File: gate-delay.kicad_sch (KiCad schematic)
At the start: 42 parts, among them J1 Conn_02x05_Odd_Even, J2 gate_in, J3 gate_out, J4 gate_out, Q1 BCM847, Q2 BSS84, Q3 MMBF170, U1 TL072

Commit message: fix: try to maintain gate duration
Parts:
- added R17, R19, R21, R22: 10K, symbol Device:R
- added R18: 68K, symbol Device:R
- added R20: 50K, symbol Device:R
- R10: value 24K -> 1K
- R11: value 47K -> 10K
- R13: value 1K -> 68K
- R14: value 10K -> 50K
- R8: value 10K -> 110K
- R9: value 10K -> 22K
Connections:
- net +12V': now also R18.1; no longer R8.1
- net -12V': now also C3.2, Q3.2 (S)
- net GND': now also R11.2, U1.2 (-), R20.2, R21.1; no longer C3.2, Q3.2 (S), R9.2
- net at D4.1 (K), Q1.5 (B2): now also R10.2; no longer R13.1
- net at D4.2 (A), U1.1: now also R9.1; no longer R11.1
- net at R13.2, R14.1: now also R17.1; no longer R16.2
- net at C3.1, RV1.2, RV1.3: now also R13.1, R8.2; no longer R10.1, U1.5 (+)
- net at R15.2, U1.7: now also R22.2; no longer U1.6 (-)
- new net: R10.1, R11.1, R16.2
- new net: R8.1, R9.2, U1.3 (+)
- new net: R21.2, R22.1, U1.6 (-)
- new net: R18.2, R19.1, R20.1
- new net: R17.2, R19.2, U1.5 (+)
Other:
- moved on the sheet: R10, R11, R13, R14, R15, R8, R9, U1B

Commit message: feat: v0 pcb layed out
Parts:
- removed R15, R16: 1K, symbol Device:R
- removed R17, R19, R21, R22: 10K, symbol Device:R
- removed R18: 68K, symbol Device:R
- removed R20: 50K, symbol Device:R
- added H9: led, Eurorack:Mech-LED-Hole-3mm-Bezel, symbol Eurorack:MountingHole_Pad_Output
- C3: footprint (none) -> Capacitor_THT:C_Rect_L7.2mm_W5.5mm_P5.00mm_FKS2_FKP2_MKS2_MKP2
- C4: footprint (none) -> Capacitor_SMD:C_0805_2012Metric
- D3, D4: footprint (none) -> Diode_SMD:D_SOD-323_HandSoldering
- D5: footprint (none) -> LED_THT:LED_D3.0mm
- H8: value slew -> delay
- J2, J3: footprint (none) -> Eurorack:AudioJack2_Tayda_A-2566
- J4: value gate_out -> slew_out; footprint (none) -> Eurorack:AudioJack2_Tayda_A-2566
- Q2: footprint Package_TO_SOT_THT:TO-92_Inline -> Package_TO_SOT_SMD:SOT-23
- R10, R11, R12, R3, R4, R5, R6, R7, R8, R9: footprint (none) -> Resistor_SMD:R_0805_2012Metric
- R13: value 68K -> 1K; footprint (none) -> Resistor_SMD:R_0805_2012Metric
- R14: value 50K -> 1K; footprint (none) -> Resistor_SMD:R_0805_2012Metric
- RV1: footprint (none) -> Eurorack:Potentiometer_RV16AF-41-15R1
- U1: footprint (none) -> Package_SO:SOIC-8_3.9x4.9mm_P1.27mm
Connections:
- net +12V' is gone; now on net +12V: C4.1, Q1.3 (C2), Q2.2 (S), R5.1, U1.8 (V+)
- net +12V: now also R8.2
- net -12V: now also C4.2, U1.4 (V-)
- net FACE: now also H9.1
- net GATE_OUT': now also R13.1
- net GND: now also C3.2, D3.2 (A), J2.S, J3.S, J4.S, Q1.1 (E1), Q3.2 (S), R11.2, R12.2, R4.2, R9.1
- net SLEW_OUT': now also R14.1
- net at D4.2 (A), U1.1: no longer R9.1
- net at R10.1, R11.1: now also R13.2
- net at C3.1, RV1.2, RV1.3: now also U1.3 (+), U1.5 (+); no longer R13.1, R8.2
- net at R8.1, R9.2: now also U1.2 (-); no longer U1.3 (+)
- net at U1.6 (-): now also R14.2, U1.7
- removed net -12V': C3.2, C4.2, Q3.2 (S), U1.4 (V-)
- removed net GND': D3.2 (A), J2.S, J3.S, J4.S, Q1.1 (E1), R11.2, R12.2, R14.2, R4.2, U1.2 (-)
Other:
- moved on the sheet: R13, R14, R8, R9, U1B

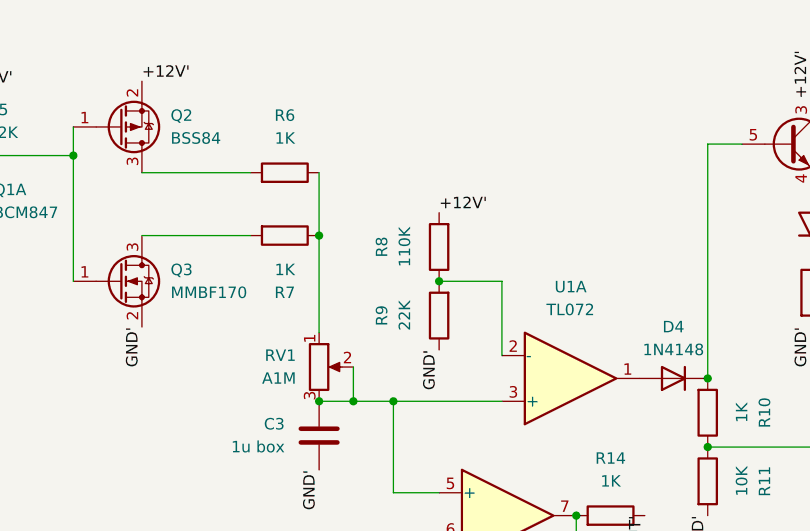
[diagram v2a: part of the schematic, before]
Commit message: v1 ready (uses the v0 board)
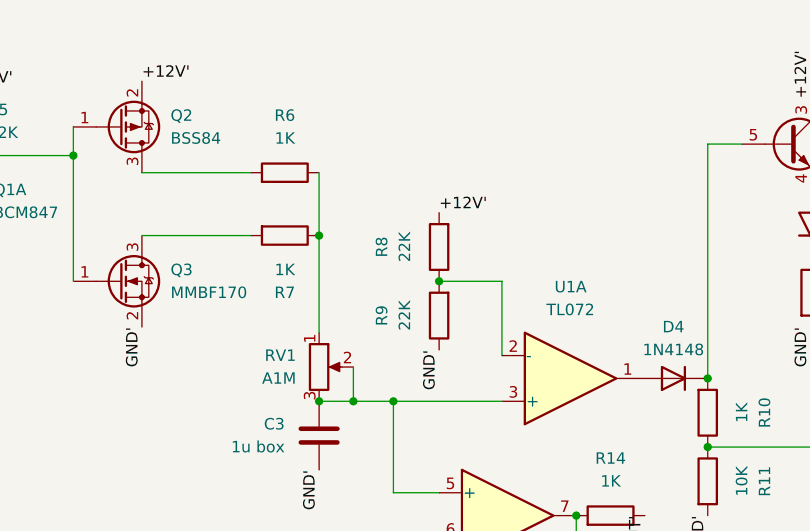
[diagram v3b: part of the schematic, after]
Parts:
- R8: value 110K -> 22K
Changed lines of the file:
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@@
       (effects (font (size 1.27 1.27)))
     )
-    (property "Value" "110K" (at 169.545 44.45 90)
+    (property "Value" "22K" (at 169.545 44.45 90)
       (effects (font (size 1.27 1.27)))
     )
